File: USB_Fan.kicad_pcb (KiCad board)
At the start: 4 copper layers, 36.4 x 25.7 mm, 38 parts, among them J1 USB-C (Female), J2 Fan, J3 Fan Voltage, SW1 Power, U1 TP4056, U2 DW01A-G, U3 FS8205A, U4 TPS61170

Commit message: Fix problems on the PCB
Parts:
- removed the C6 at (103.7, 50.8)
- removed L2: 10uH, Custom:Inductor 4x4
- R7: footprint Resistor_SMD:R_0805_2012Metric -> Resistor_SMD:R_0603_1608Metric
- moved D1 2.26 mm to (103.9, 51.8), turned to 90 degrees
- moved SW1 1.62 mm to (106.7, 40.6)
- moved H4 1.41 mm to (111.3, 39.6)
- moved J2 1.39 mm to (110.5, 48.1)
- moved BT1 1.31 mm to (110.5, 57.7)
- moved U3 1.31 mm to (96.0, 58.7)
- moved C3 1.31 mm to (104.4, 57.9)
- moved R6 1.31 mm to (99.4, 55.4)
- moved U2 1.31 mm to (101.3, 58.7)
- moved U1 1.21 mm to (90.5, 55.4)
- moved C1 1.21 mm to (89.0, 50.9)
- moved C2 1.21 mm to (86.9, 56.5)
- moved R5 1.21 mm to (92.0, 50.9)
- moved C6 1.08 mm to (105.9, 52.6), turned to -90 degrees
- moved R7 1.08 mm to (106.2, 59.4), turned to 90 degrees
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- renumbered C7 to C6
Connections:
- L1 pad 2: Net-(U4-SW) -> Net-(D1-A)
- U4 pad 4: Net-(U4-SW) -> Net-(D1-A)
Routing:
- net Net-(U4-SW): track 4.86 -> 0.00 mm
- net +BATT: track 67.3 -> 63.9 mm
- net /Standby: track 10.8 -> 9.25 mm
- net Net-(SW1-A): track 13.6 -> 12.2 mm
- net /V_{OUT}: track 35.6 -> 34.3 mm
- net GND: track 27.8 -> 26.6 mm, vias 35 -> 43
- net Net-(D1-A): track 3.88 -> 5.06 mm
- net +5V: track 40.8 -> 39.6 mm
- net /Charging: track 10.6 -> 9.71 mm
- net /DW01A Vcc: track 3.69 -> 4.38 mm
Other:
- board size 36.4 x 25.7 mm -> 35.1 x 24.9 mm

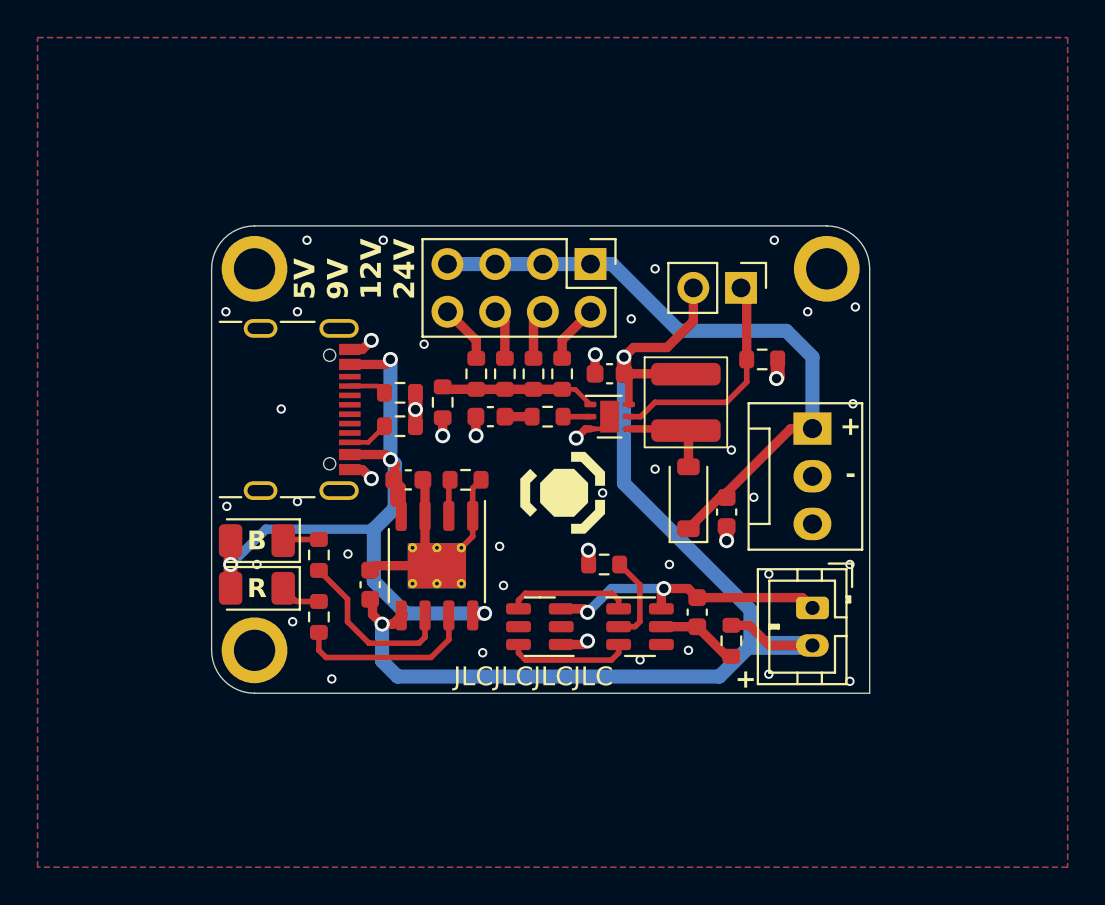
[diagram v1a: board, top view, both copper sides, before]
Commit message: Add tooling holes
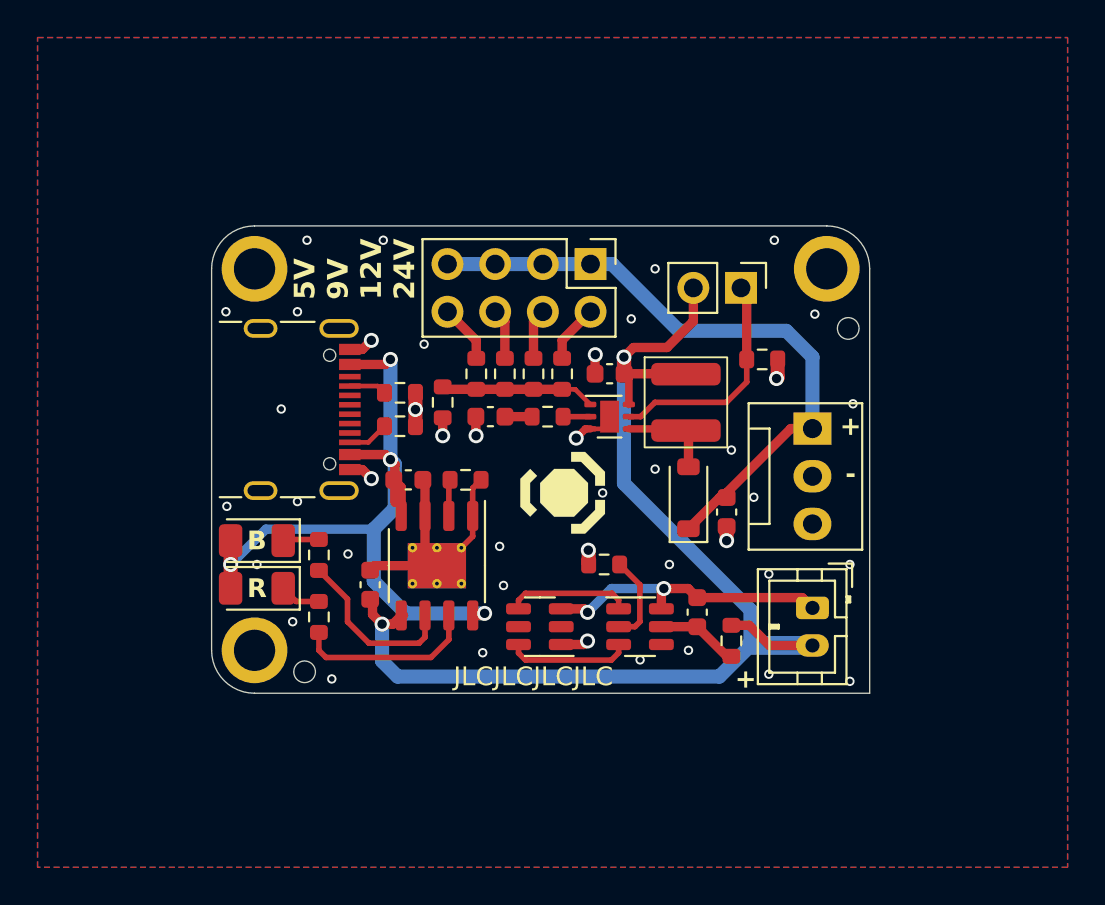
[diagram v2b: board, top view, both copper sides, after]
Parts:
- added H1: MountingHole_Pad, Custom:JLCPCB ToolingHole, F.Cu at (83.4, 61.1)
- added H2: MountingHole_Pad, Custom:JLCPCB ToolingHole, F.Cu at (112.4, 42.8)
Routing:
- net GND: vias 43 -> 42
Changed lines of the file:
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@@
 (kicad_pcb (version 20221018) (generator pcbnew)
   (general
-    (thickness 1.6)
+    (thickness 1.2)
   )
   (paper "A5")
@@
       (layer "F.Mask" (type "Top Solder Mask") (color "Blue") (thickness 0.01))
       (layer "F.Cu" (type "copper") (thickness 0.035))
-      (layer "dielectric 1" (type "core") (thickness 0.48) (material "FR4") (epsilon_r 4.5) (loss_tangent 0.02))
+      (layer "dielectric 1" (type "prepreg") (thickness 0.1) (material "FR4") (epsilon_r 4.5) (loss_tangent 0.02))
       (layer "In1.Cu" (type "copper") (thickness 0.035))
-      (layer "dielectric 2" (type "prepreg") (thickness 0.48) (material "FR4") (epsilon_r 4.5) (loss_tangent 0.02))
+      (layer "dielectric 2" (type "core") (thickness 0.84) (material "FR4") (epsilon_r 4.5) (loss_tangent 0.02))
       (layer "In2.Cu" (type "copper") (thickness 0.035))
-      (layer "dielectric 3" (type "core") (thickness 0.48) (material "FR4") (epsilon_r 4.5) (loss_tangent 0.02))
+      (layer "dielectric 3" (type "prepreg") (thickness 0.1) (material "FR4") (epsilon_r 4.5) (loss_tangent 0.02))
       (layer "B.Cu" (type "copper") (thickness 0.035))
       (layer "B.Mask" (type "Bottom Solder Mask") (color "Blue") (thickness 0.01))
@@
     )
   )
+  (footprint "Custom:JLCPCB ToolingHole" (layer "F.Cu")
+    (at 83.439 61.087)
+    (property "LCSC" "")
+    (property "Sheetfile" "USB_Fan.kicad_sch")
+    (property "Sheetname" "")
+    (property "exclude_from_bom" "")
+    (property "ki_description" "Mounting Hole without connection")
+    (property "ki_keywords" "mounting hole")
+    (attr exclude_from_bom)
+    (fp_text reference "H1" (at 0 -1.27 unlocked) (layer "F.SilkS") hide
+        (effects (font (size 1 1) (thickness 0.1)))
+    )
+    (fp_text value "MountingHole_Pad" (at 0 1.27 unlocked) (layer "F.Fab")
+        (effects (font (size 1 1) (thickness 0.15)))
+    )
+    (fp_text user "${REFERENCE}" (at 0 2.77 unlocked) (layer "F.Fab")
+        (effects (font (size 1 1) (thickness 0.15)))
+    )
+    (pad "" np_thru_hole circle (at 0 0) (size 1.152 1.152) (drill 1.152) (layers "F&B.Cu" "*.Mask")
+      (solder_mask_margin 0.148))
+  )
+  (footprint "Custom:JLCPCB ToolingHole" (layer "F.Cu")
+    (at 112.395 42.799)
+    (property "LCSC" "")
+    (property "Sheetfile" "USB_Fan.kicad_sch")
+    (property "Sheetname" "")
+    (property "exclude_from_bom" "")
+    (property "ki_description" "Mounting Hole without connection")
+    (property "ki_keywords" "mounting hole")
+    (attr exclude_from_bom)
+    (fp_text reference "H2" (at 0 -1.27 unlocked) (layer "F.SilkS") hide
+        (effects (font (size 1 1) (thickness 0.1)))
+    )
+    (fp_text value "MountingHole_Pad" (at 0 1.27 unlocked) (layer "F.Fab")
+        (effects (font (size 1 1) (thickness 0.15)))
+    )
+    (fp_text user "${REFERENCE}" (at 0 2.77 unlocked) (layer "F.Fab")
+        (effects (font (size 1 1) (thickness 0.15)))
+    )
+    (pad "" np_thru_hole circle (at 0 0) (size 1.152 1.152) (drill 1.152) (layers "F&B.Cu" "*.Mask")
+      (solder_mask_margin 0.148))
+  )
   (footprint "MountingHole:MountingHole_2.2mm_M2_ISO7380_Pad" (layer "F.Cu")
     (at 80.772 59.944)
@@
   (segment (start 99.685 47.879) (end 99.416 48.148) (width 0.25) (layer "F.Cu") (net 1))
   (via (at 83.058 52.0192) (size 0.5) (drill 0.3) (layers "F.Cu" "B.Cu") (free) (net 1))
-  (via (at 110.236 41.91) (size 0.5) (drill 0.3) (layers "F.Cu" "B.Cu") (free) (net 1))
+  (via (at 110.617 42.037) (size 0.5) (drill 0.3) (layers "F.Cu" "B.Cu") (free) (net 1))
   (via (at 79.2988 52.2732) (size 0.5) (drill 0.3) (layers "F.Cu" "B.Cu") (free) (net 1))
   (via (at 102.108 39.624) (size 0.5) (drill 0.3) (layers "F.Cu" "B.Cu") (free) (net 1))
@@
   (via (at 92.926 60.071) (size 0.5) (drill 0.3) (layers "F.Cu" "B.Cu") (free) (net 1))
   (via (at 86.995 50.8) (size 0.8) (drill 0.5) (layers "F.Cu" "B.Cu") (net 1))
-  (via (at 112.776 41.656) (size 0.5) (drill 0.3) (layers "F.Cu" "B.Cu") (free) (net 1))
   (via (at 93.8276 54.4068) (size 0.5) (drill 0.3) (layers "F.Cu" "B.Cu") (free) (net 1))
   (via (at 89.8044 43.6372) (size 0.5) (drill 0.3) (layers "F.Cu" "B.Cu") (free) (net 1))

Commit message: Minor tweaks to the PCB
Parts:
- moved C6 0.25 mm to (105.9, 52.8)
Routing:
- net +5V: track 39.6 -> 38.4 mm
- net GND: track 26.6 -> 27.3 mm, vias 42 -> 41
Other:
- board text added: "Standby Charging"
